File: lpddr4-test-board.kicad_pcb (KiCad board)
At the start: 8 copper layers, 117 x 86 mm, 266 parts, among them IC1 TPS54561, IC3 TPD8S009DSMR, J1 0878311420, J10 61300311121, J2 08B0-1X1T-36-F, J3 DC_SOCKET, J4 WE_629105150521, J5 2309409-1, J6 685119134923, J7 1140084168, Q2 BSS138APW, Q3 BSS138APW, Q4 BSS138APW, Q5 BSS138APW, Q6 BSS138APW, Q7 BSS138APW, Q8 BSS138APW, U1 XC7K70T-FBG484, U2 ASEM1-100.000MHZ-LC-T, U3 S25FL128SAGNFI000, U4 TPS65296, U5 TPS62823DLCT, U6 DP83848JSQ_NOPB, U7 FT4232HQ, Y1 ABM8G-25.000MHZ-18-D2Y-T

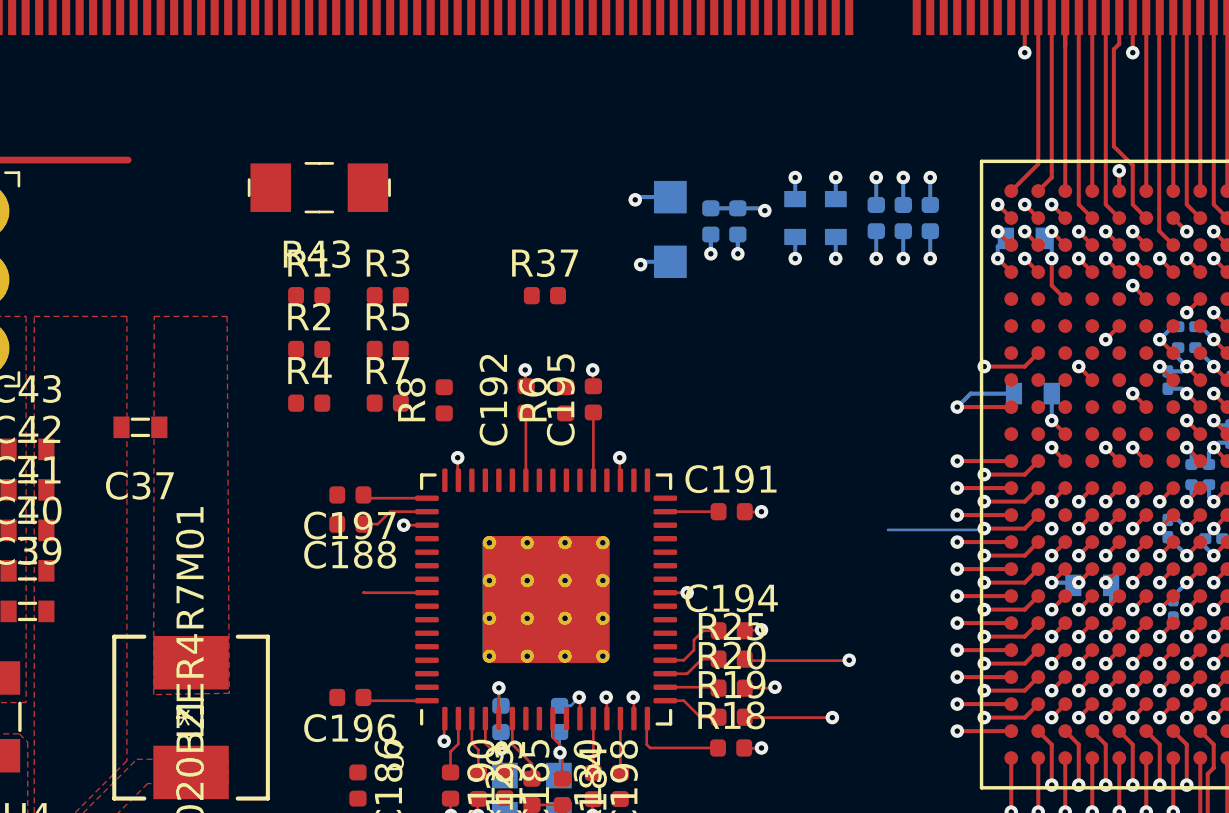
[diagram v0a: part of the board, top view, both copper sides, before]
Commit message: Routed FTDI signals towards FPGA balls
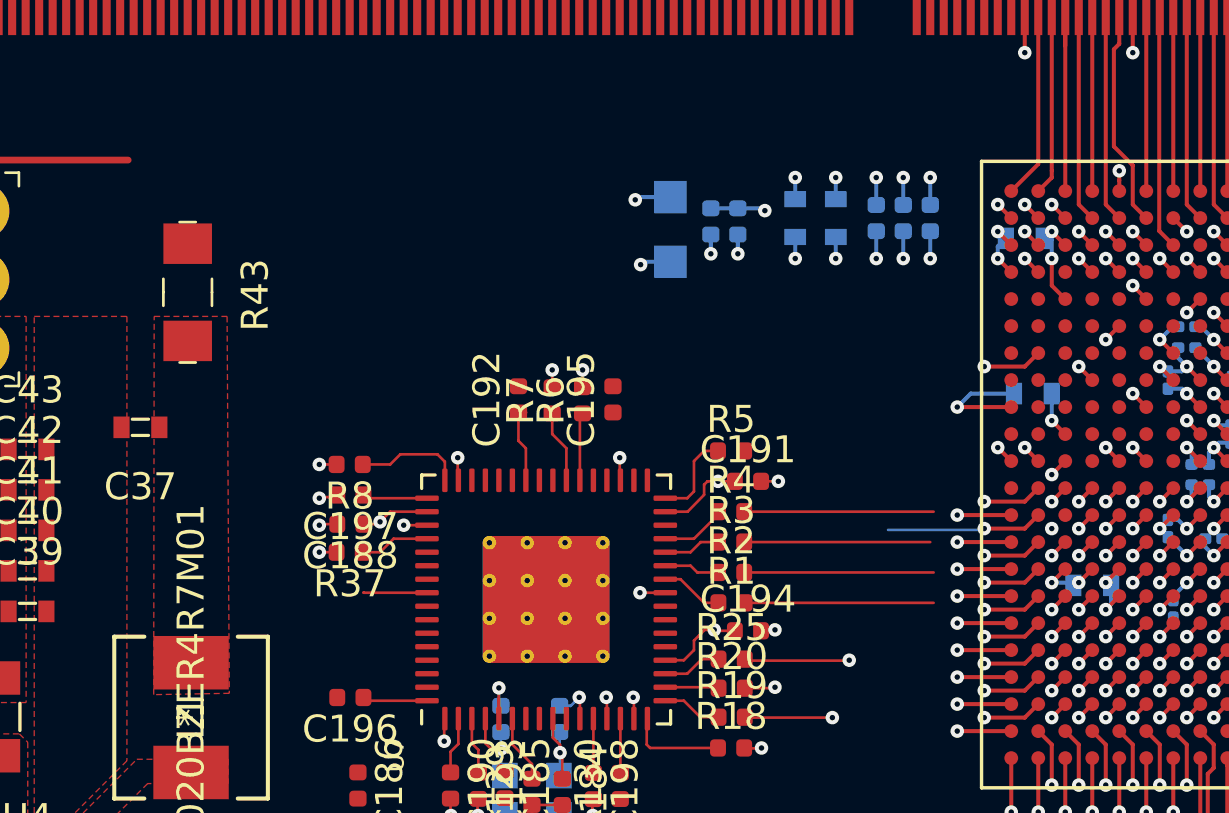
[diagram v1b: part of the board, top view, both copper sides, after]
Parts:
- moved R1 19.3 mm to (148.2, 100.7)
- moved R2 17.7 mm to (148.2, 99.6)
- moved R4 16.1 mm to (148.2, 97.4)
- moved R3 15.7 mm to (148.2, 98.5)
- moved R5 13.3 mm to (148.2, 95.1)
- moved R37 11.9 mm to (134.0, 98.9), turned to 180 degrees
- moved R43 6.23 mm to (128.0, 89.2), turned to 270 degrees
- moved R7 6.09 mm to (141.5, 93.2), turned to 90 degrees
- moved R8 4.23 mm to (134.0, 95.6), turned to 180 degrees
- moved C191 1.28 mm to (148.8, 96.2)
- moved C195 0.72 mm to (143.8, 93.2)
- moved R6 0.62 mm to (142.7, 93.2)
- moved C194 0.60 mm to (148.8, 101.8)
- moved C192 0.28 mm to (140.3, 93.2)
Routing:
- net UART1_RX: track 0.00 -> 24.2 mm, vias 0 -> 1
- net UART1_TX: track 0.00 -> 24.0 mm, vias 0 -> 1
- net UART0_TX: track 0.00 -> 21.5 mm, vias 0 -> 1
- net UART0_RX: track 0.00 -> 19.7 mm, vias 0 -> 1
- net AUX_JTAG_TMS: track 0.00 -> 7.01 mm
- net AUX_JTAG_TDI: track 0.00 -> 7.01 mm
- net AUX_JTAG_TCK: track 0.00 -> 7.01 mm
- net AUX_JTAG_TDO: track 0.00 -> 6.89 mm
- net Net-(R8-Pad1): track 0.00 -> 4.00 mm
- net Net-(R5-Pad1): track 0.00 -> 3.34 mm
- net Net-(R7-Pad1): track 0.00 -> 2.69 mm
- net Net-(R37-Pad1): track 0.00 -> 2.58 mm
- net Net-(R6-Pad1): track 0.00 -> 2.52 mm
- net VCC1V8: track 27.2 -> 24.7 mm
- net Net-(R4-Pad1): track 0.00 -> 2.43 mm
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
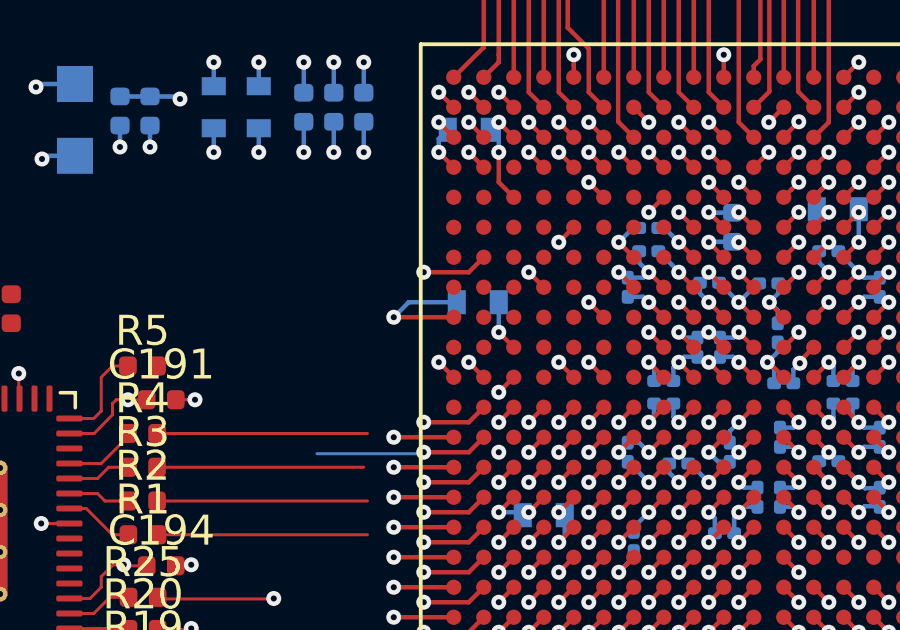
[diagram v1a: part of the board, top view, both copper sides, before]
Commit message: Update C24 routing
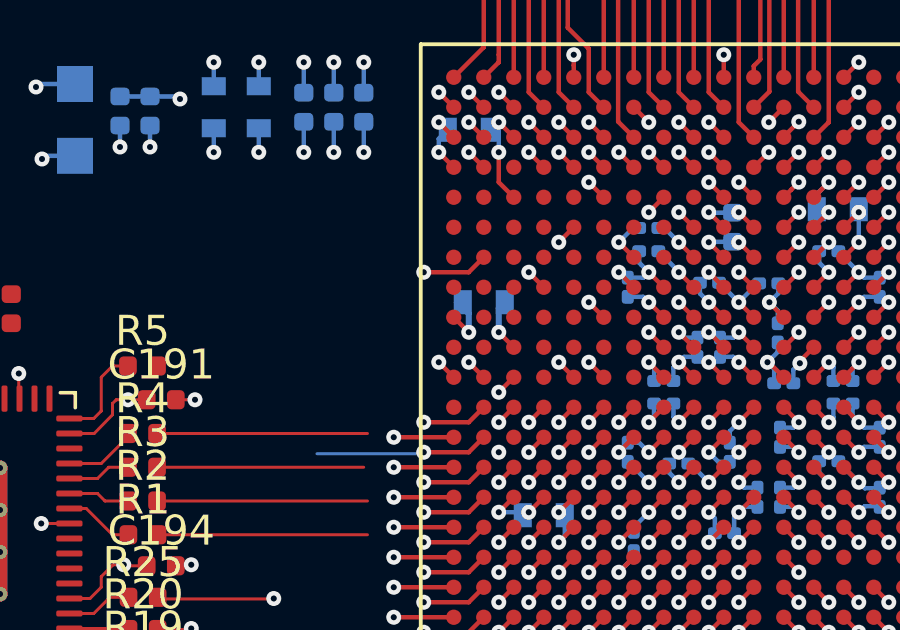
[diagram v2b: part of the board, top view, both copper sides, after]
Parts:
- moved C24 0.20 mm to (159.5, 93.0)
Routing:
- net GND: track 216.2 -> 213.8 mm
- net UART0_TX: track 21.5 -> 21.0 mm

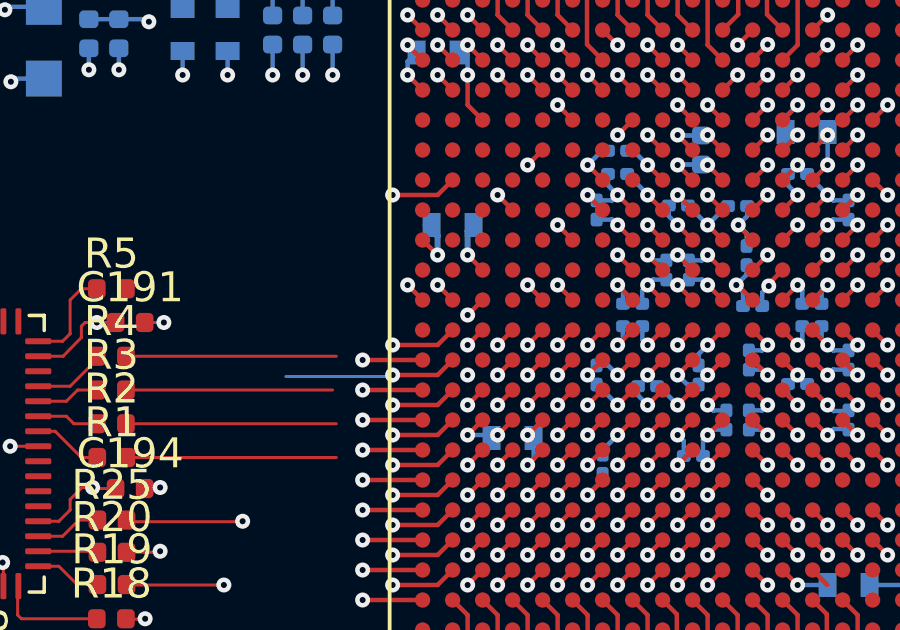
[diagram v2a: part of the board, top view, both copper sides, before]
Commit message: Reconnect FTDI UART lanes
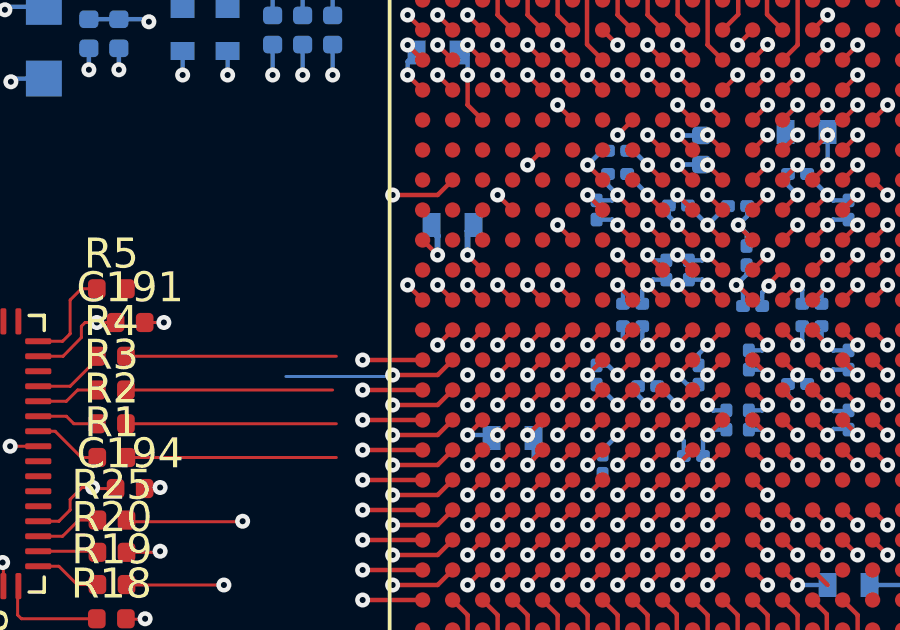
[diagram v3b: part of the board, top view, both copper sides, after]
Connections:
- U1 pad AA11: Net-(U1-PadAA11) -> UART0_TX
- U1 pad AB11: Net-(U1-PadAB11) -> UART0_RX
- U1 pad W11: Net-(U1-PadW11) -> UART1_TX
- U1 pad Y11: Net-(U1-PadY11) -> UART1_RX
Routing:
- net UART1_TX: track 24.0 -> 31.1 mm, vias 1 -> 2
- net UART1_RX: track 24.2 -> 30.1 mm, vias 1 -> 2
- net UART0_TX: track 21.0 -> 23.9 mm, vias 1 -> 2
- net UART0_RX: track 19.7 -> 21.6 mm, vias 1 -> 2
- net GND: track 213.8 -> 212.3 mm
- net Net-(U1-PadY11): track 0.71 -> 0.00 mm, vias 1 -> 0
- net Net-(U1-PadAB11): track 0.71 -> 0.00 mm, vias 1 -> 0
- net Net-(U1-PadAA11): track 0.71 -> 0.00 mm, vias 1 -> 0

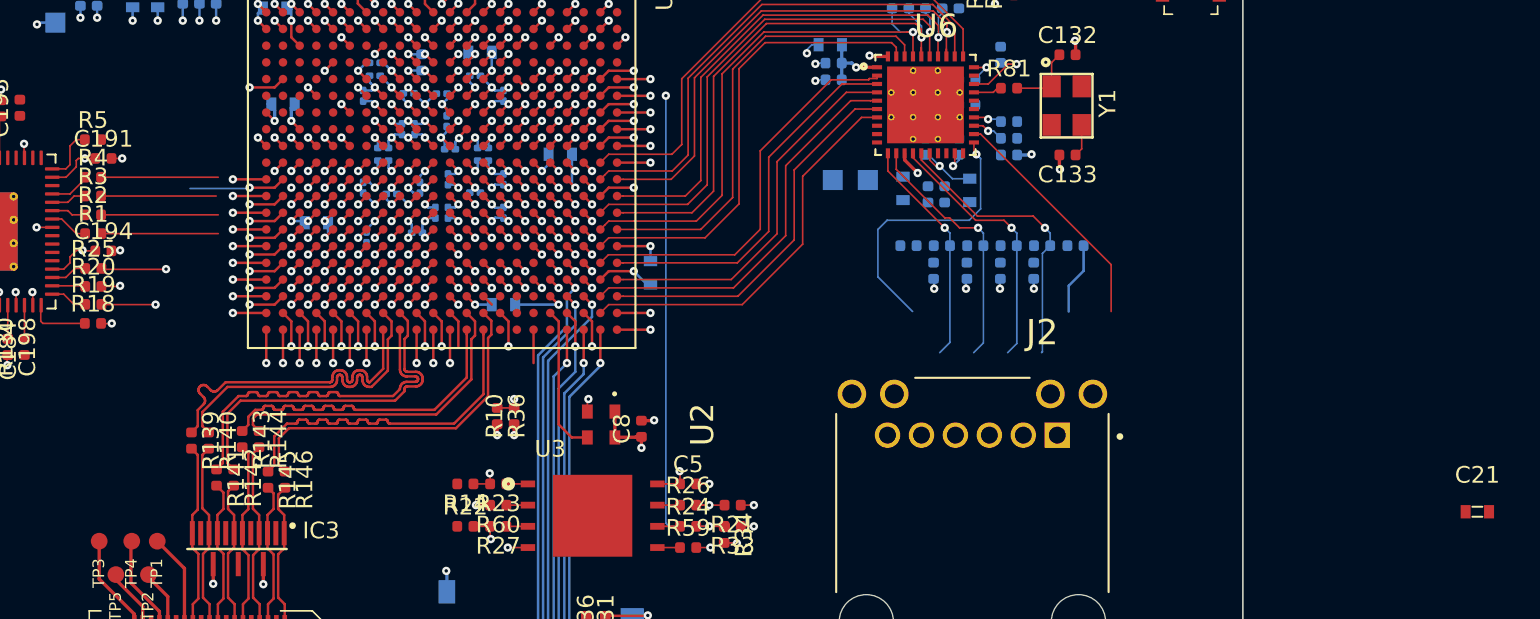
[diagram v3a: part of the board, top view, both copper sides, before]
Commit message: Connect remaining AUX JTAG signals
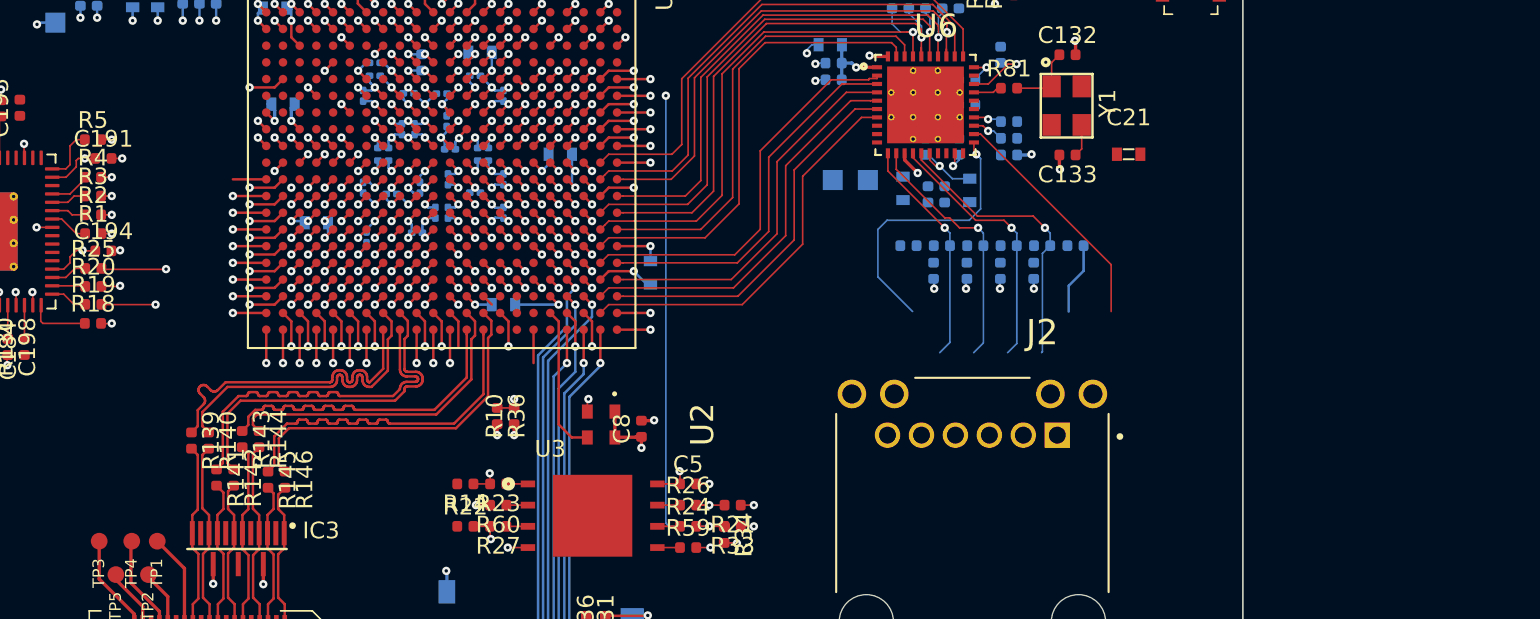
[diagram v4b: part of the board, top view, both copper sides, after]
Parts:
- moved C21 29.9 mm to (210.2, 96.0)
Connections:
- U1 pad AB10: Net-(U1-PadAB10) -> AUX_JTAG_RST
- U1 pad U12: Net-(U1-PadU12) -> AUX_JTAG_TCK
- U1 pad V12: Net-(U1-PadV12) -> AUX_JTAG_TDI
- U1 pad W12: Net-(U1-PadW12) -> AUX_JTAG_TDO
- U1 pad Y12: Net-(U1-PadY12) -> AUX_JTAG_TMS
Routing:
- net AUX_JTAG_TCK: track 7.01 -> 18.3 mm, vias 0 -> 2
- net AUX_JTAG_RST: track 0.00 -> 10.9 mm, vias 0 -> 2
- net AUX_JTAG_TDI: track 7.01 -> 16.8 mm, vias 0 -> 2
- net AUX_JTAG_TDO: track 6.89 -> 15.4 mm, vias 0 -> 2
- net AUX_JTAG_TMS: track 7.01 -> 13.7 mm, vias 0 -> 2
- net Net-(U1-PadAA13): track 5.79 -> 2.28 mm
- net Net-(U1-PadY12): track 0.71 -> 0.00 mm, vias 1 -> 0
- net Net-(U1-PadU12): track 0.71 -> 0.00 mm, vias 1 -> 0
- net Net-(U1-PadW12): track 0.71 -> 0.00 mm, vias 1 -> 0
- net Net-(U1-PadV12): track 0.71 -> 0.00 mm, vias 1 -> 0
- net Net-(U1-PadAB13): vias 1 -> 0

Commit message: Connected RGMII - Wip
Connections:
- net Net-(U1-PadC13) renamed ETH_TX_RSTN
- U1 pad C12: Net-(U1-PadC12) -> ETH_MDIO
- U1 pad C14: Net-(U1-PadC14) -> ETH_MDC
- U1 pad C15: Net-(U1-PadC15) -> ETH_REF_CLK
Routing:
- net ETH_REF_CLK: track 0.00 -> 28.4 mm, vias 0 -> 2
- net ETH_MDC: track 0.00 -> 25.9 mm, vias 0 -> 2
- net ETH_MDIO: track 1.72 -> 26.5 mm, vias 1 -> 2
- net VCC3V3: track 80.5 -> 79.0 mm
- net ETH_TX_RSTN: track 0.71 -> 1.46 mm
- net Net-(U1-PadC15): track 0.71 -> 0.00 mm, vias 1 -> 0
- net Net-(U1-PadC14): track 0.71 -> 0.00 mm, vias 1 -> 0
- net Net-(U1-PadC12): track 0.71 -> 0.00 mm, vias 1 -> 0
